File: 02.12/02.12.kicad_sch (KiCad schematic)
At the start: 110 parts

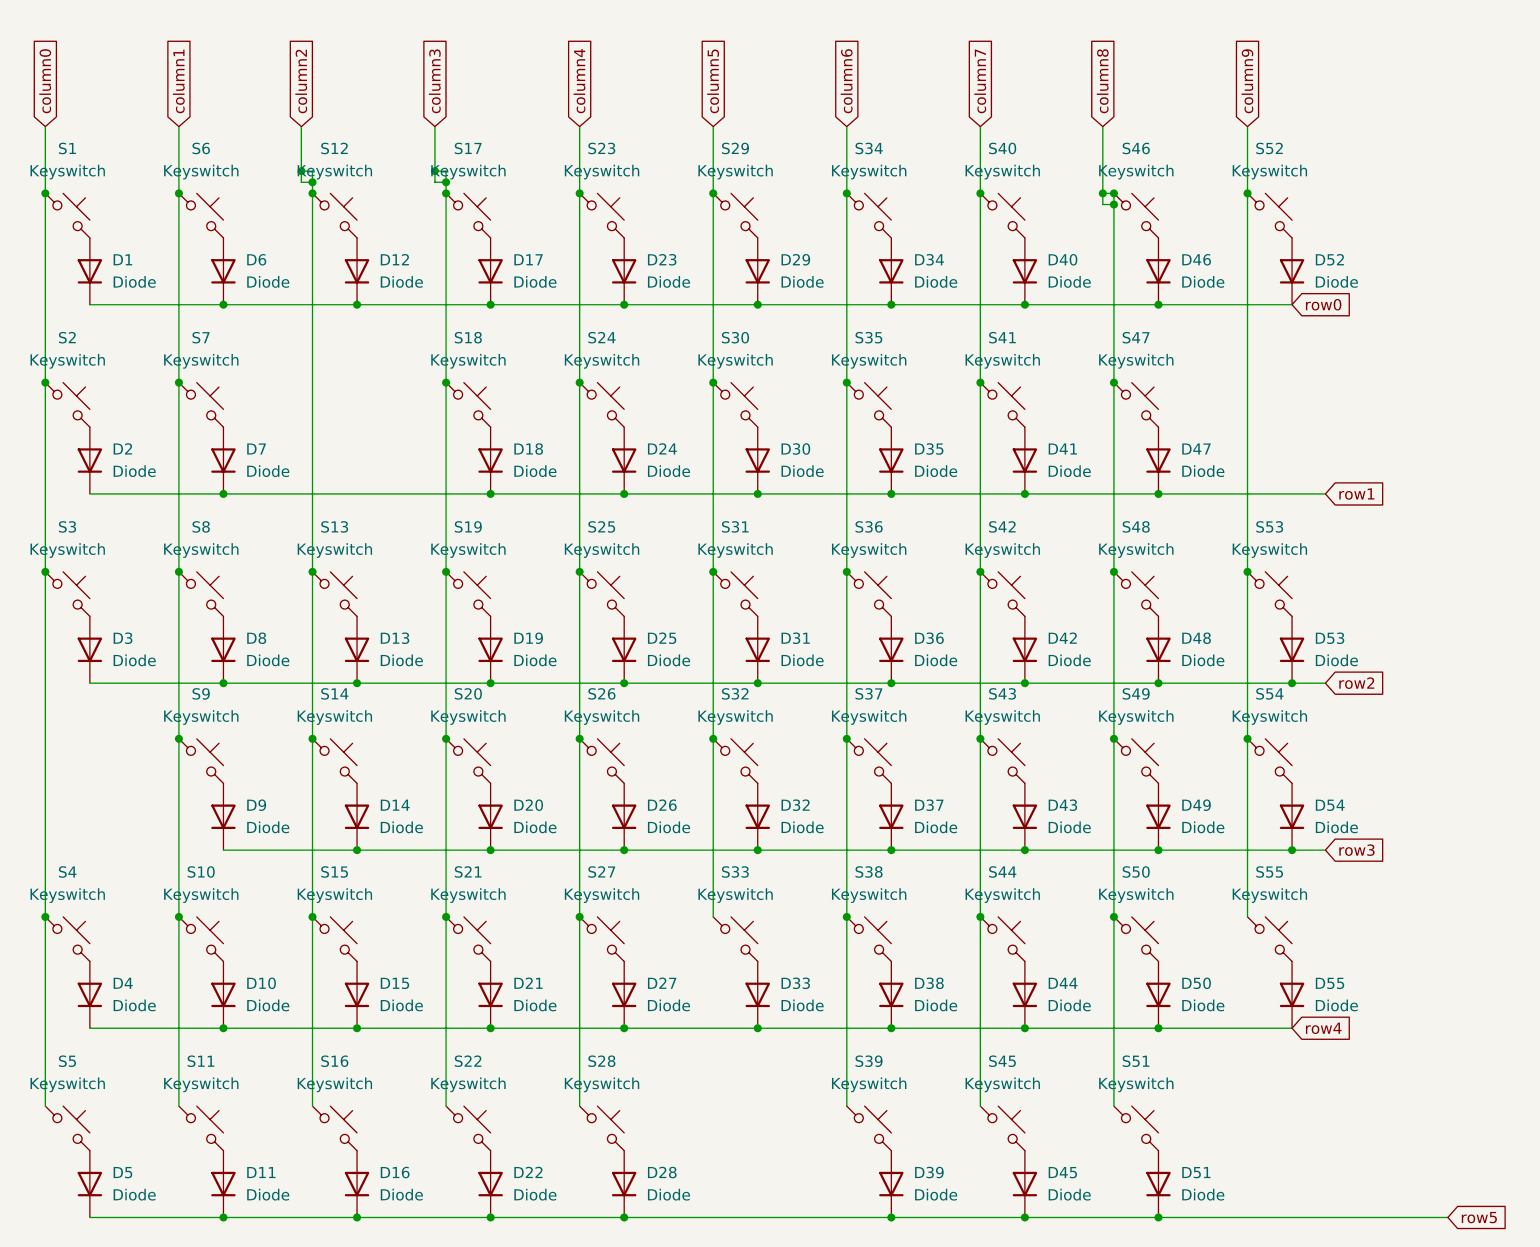
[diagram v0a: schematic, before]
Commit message: add layout for keyboard
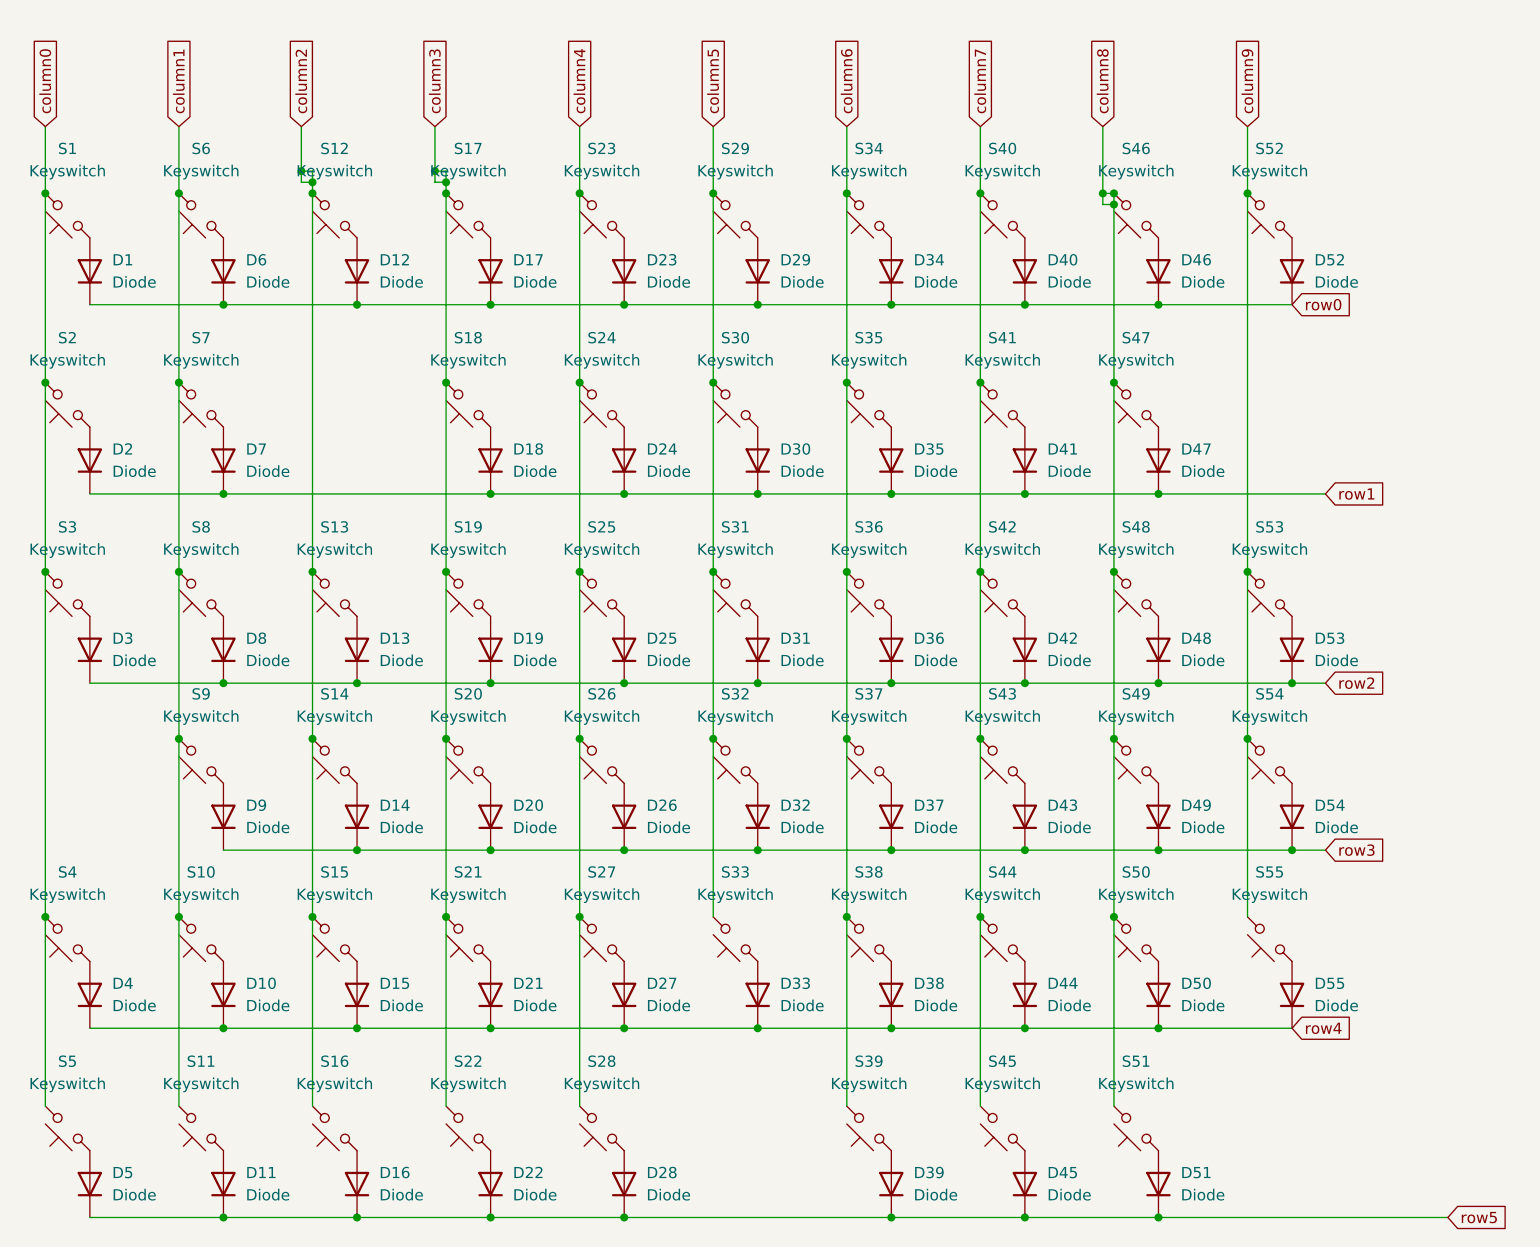
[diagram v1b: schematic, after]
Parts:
- S1, S10, S11, S12, S13, S14, S15, S16, S17, S18, S19, S2, S20, S21, S22, S23, S24, S25, S26, S27, S28, S29, S3, S30, S31, S32, S33, S34, S35, S36, S37, S38, S39, S4, S40, S41, S42, S43, S44, S45, S46, S47, S48, S49, S5, S50, S51, S52, S53, S54, S55, S6, S7, S8, S9: footprint DomeSwitches:DomeSwitch_8mm_double_sided -> Dome_05_30:dome_05_30
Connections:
- net column0: now also S1.2, S2.2, S3.2, S4.2, S5.2; no longer S1.1, S2.1, S3.1, S4.1, S5.1
- net column1: now also S10.2, S11.2, S6.2, S7.2, S8.2, S9.2; no longer S10.1, S11.1, S6.1, S7.1, S8.1, S9.1
- net column2: now also S12.2, S13.2, S14.2, S15.2, S16.2; no longer S12.1, S13.1, S14.1, S15.1, S16.1
- net column3: now also S17.2, S18.2, S19.2, S20.2, S21.2, S22.2; no longer S17.1, S18.1, S19.1, S20.1, S21.1, S22.1
- net column4: now also S23.2, S24.2, S25.2, S26.2, S27.2, S28.2; no longer S23.1, S24.1, S25.1, S26.1, S27.1, S28.1
- net column5: now also S29.2, S30.2, S31.2, S32.2, S33.2; no longer S29.1, S30.1, S31.1, S32.1, S33.1
- net column6: now also S34.2, S35.2, S36.2, S37.2, S38.2, S39.2; no longer S34.1, S35.1, S36.1, S37.1, S38.1, S39.1
- net column7: now also S40.2, S41.2, S42.2, S43.2, S44.2, S45.2; no longer S40.1, S41.1, S42.1, S43.1, S44.1, S45.1
- net column8: now also S46.2, S47.2, S48.2, S49.2, S50.2, S51.2; no longer S46.1, S47.1, S48.1, S49.1, S50.1, S51.1
- net column9: now also S52.2, S53.2, S54.2, S55.2; no longer S52.1, S53.1, S54.1, S55.1
- net at D44.2 (A): now also S44.1; no longer S44.2
- net at D53.2 (A): now also S53.1; no longer S53.2
- net at D27.2 (A): now also S27.1; no longer S27.2
- net at D16.2 (A): now also S16.1; no longer S16.2
- net at D51.2 (A): now also S51.1; no longer S51.2
- net at D37.2 (A): now also S37.1; no longer S37.2
- net at D35.2 (A): now also S35.1; no longer S35.2
- net at D10.2 (A): now also S10.1; no longer S10.2
- net at D49.2 (A): now also S49.1; no longer S49.2
- net at D47.2 (A): now also S47.1; no longer S47.2
- net at D22.2 (A): now also S22.1; no longer S22.2
- net at D24.2 (A): now also S24.1; no longer S24.2
- net at D14.2 (A): now also S14.1; no longer S14.2
- net at D29.2 (A): now also S29.1; no longer S29.2
- net at D5.2 (A): now also S5.1; no longer S5.2
- net at D26.2 (A): now also S26.1; no longer S26.2
- net at D6.2 (A): now also S6.1; no longer S6.2
- net at D21.2 (A): now also S21.1; no longer S21.2
- net at D33.2 (A): now also S33.1; no longer S33.2
- net at D50.2 (A): now also S50.1; no longer S50.2
- net at D3.2 (A): now also S3.1; no longer S3.2
- net at D39.2 (A): now also S39.1; no longer S39.2
- net at D8.2 (A): now also S8.1; no longer S8.2
- net at D34.2 (A): now also S34.1; no longer S34.2
- net at D12.2 (A): now also S12.1; no longer S12.2
- net at D1.2 (A): now also S1.1; no longer S1.2
- net at D48.2 (A): now also S48.1; no longer S48.2
- net at D13.2 (A): now also S13.1; no longer S13.2
- net at D25.2 (A): now also S25.1; no longer S25.2
- net at D7.2 (A): now also S7.1; no longer S7.2
- net at D20.2 (A): now also S20.1; no longer S20.2
- net at D40.2 (A): now also S40.1; no longer S40.2
- net at D19.2 (A): now also S19.1; no longer S19.2
- net at D55.2 (A): now also S55.1; no longer S55.2
- net at D18.2 (A): now also S18.1; no longer S18.2
- net at D4.2 (A): now also S4.1; no longer S4.2
- net at D9.2 (A): now also S9.1; no longer S9.2
- net at D11.2 (A): now also S11.1; no longer S11.2
- net at D43.2 (A): now also S43.1; no longer S43.2
- net at D17.2 (A): now also S17.1; no longer S17.2
- net at D30.2 (A): now also S30.1; no longer S30.2
- net at D28.2 (A): now also S28.1; no longer S28.2
- net at D36.2 (A): now also S36.1; no longer S36.2
- net at D42.2 (A): now also S42.1; no longer S42.2
- net at D52.2 (A): now also S52.1; no longer S52.2
- net at D2.2 (A): now also S2.1; no longer S2.2
- net at D54.2 (A): now also S54.1; no longer S54.2
- net at D38.2 (A): now also S38.1; no longer S38.2
- net at D31.2 (A): now also S31.1; no longer S31.2
- net at D46.2 (A): now also S46.1; no longer S46.2
- net at D23.2 (A): now also S23.1; no longer S23.2
- net at D32.2 (A): now also S32.1; no longer S32.2
- net at D41.2 (A): now also S41.1; no longer S41.2
- net at D15.2 (A): now also S15.1; no longer S15.2
- net at D45.2 (A): now also S45.1; no longer S45.2
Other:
- moved on the sheet: S1, S10, S11, S12, S13, S14, S15, S16, S17, S18, S19, S2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
